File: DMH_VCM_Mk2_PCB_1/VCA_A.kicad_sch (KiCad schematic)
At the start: 19 parts, among them Q1 BC548, Q2 BC548, U1 TL074

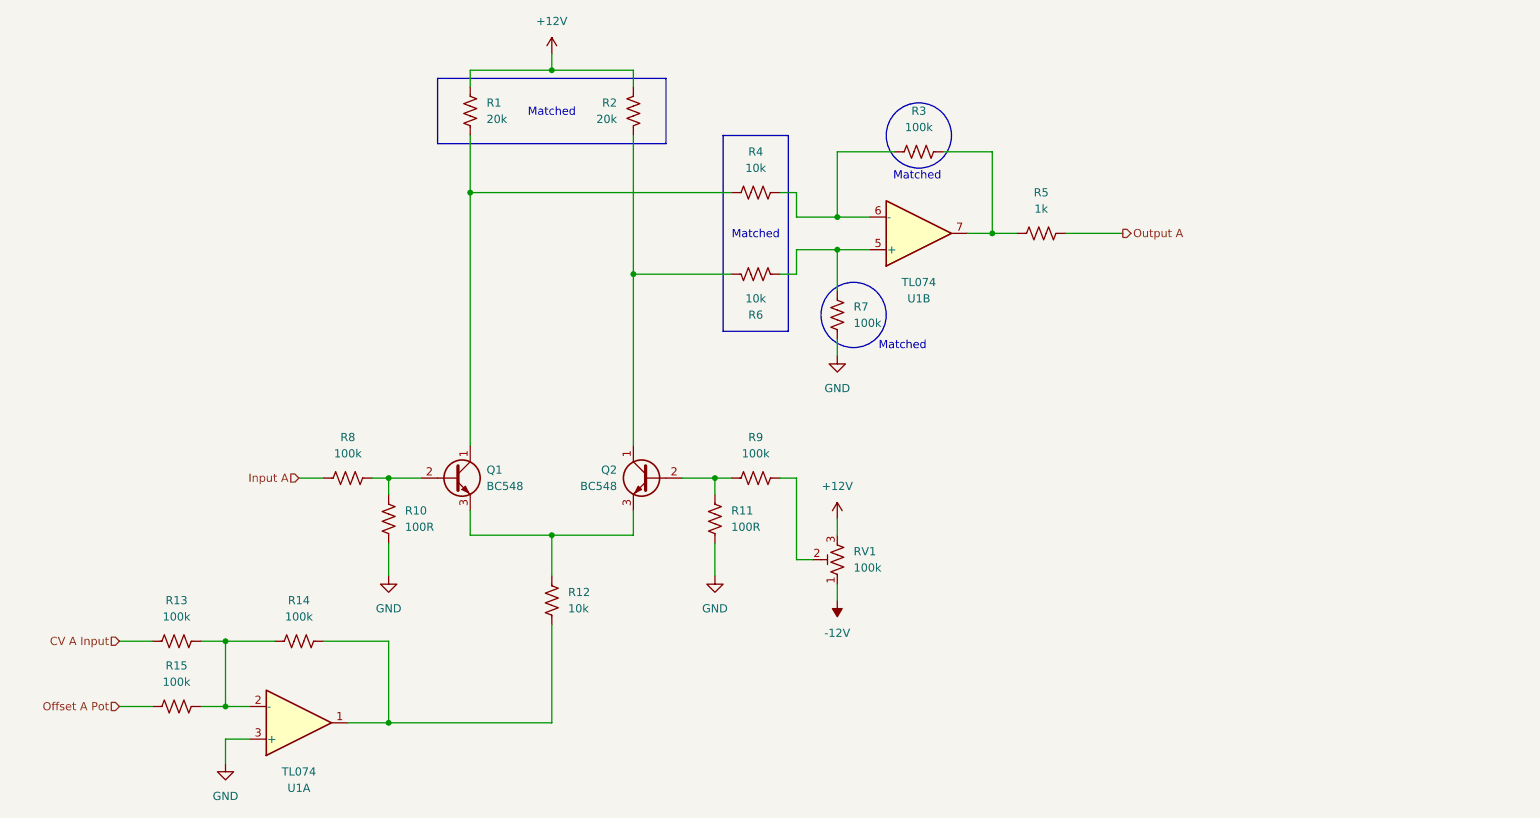
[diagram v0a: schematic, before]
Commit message: Almost finished PCB 1 schematic
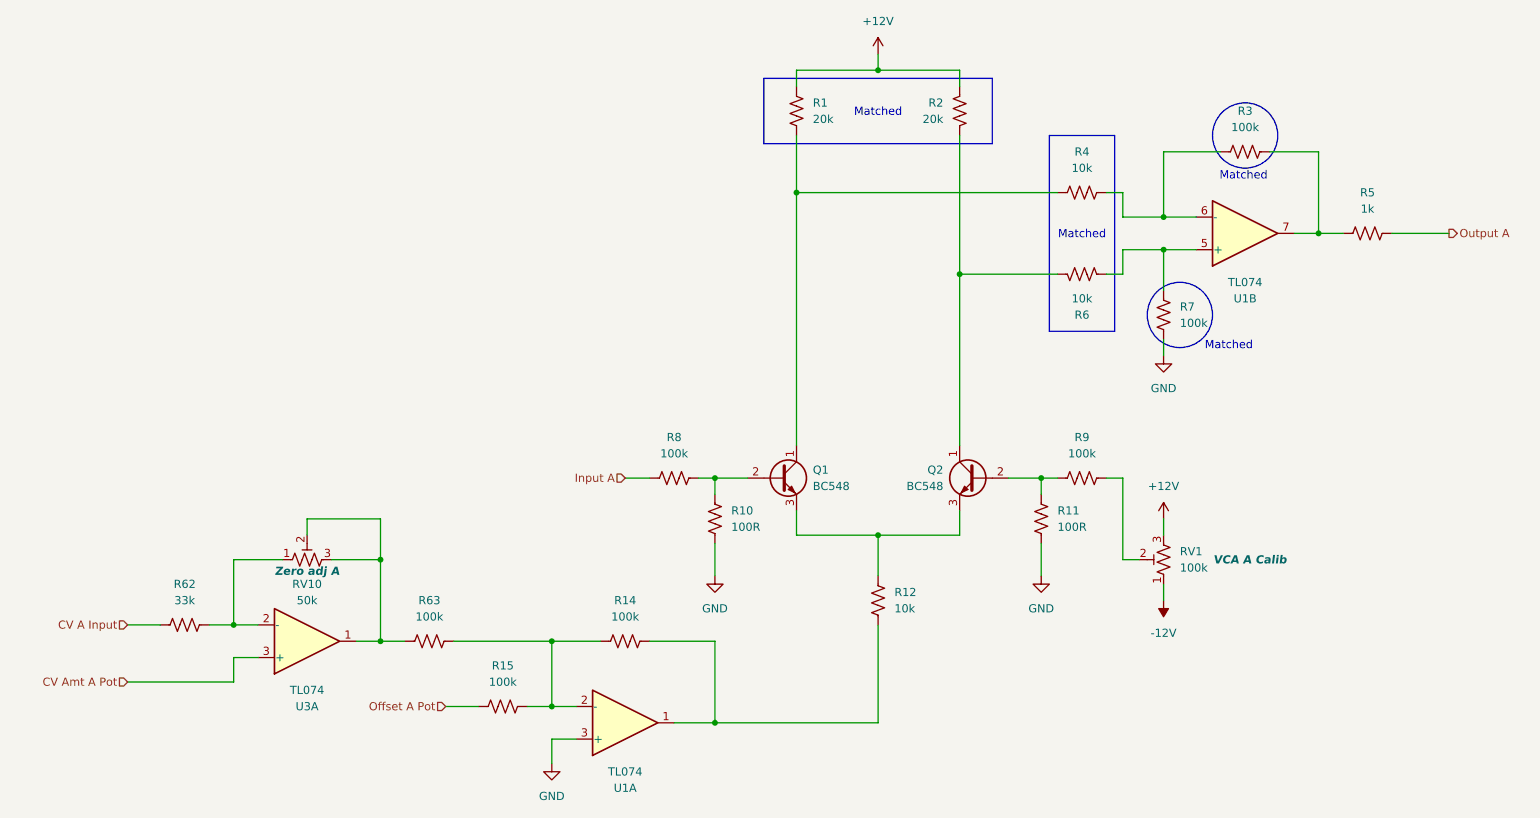
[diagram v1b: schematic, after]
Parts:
- removed R13: 100k, Resistor_THT:R_Axial_DIN0207_L6.3mm_D2.5mm_P2.54mm_Vertical, symbol Device:R_US
- added R62: 33k, Resistor_THT:R_Axial_DIN0207_L6.3mm_D2.5mm_P7.62mm_Horizontal, symbol Device:R_US
- added R63: 100k, Resistor_THT:R_Axial_DIN0207_L6.3mm_D2.5mm_P7.62mm_Horizontal, symbol Device:R_US
- added RV10: 50k, Potentiometer_THT:Potentiometer_Bourns_3296W_Vertical, symbol Device:R_Potentiometer_Trim_US
- added U3: TL074, Package_DIP:DIP-14_W7.62mm_Socket, symbol Amplifier_Operational:TL074
- RV1: Function (none) -> VCA A Calib
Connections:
- net CV A Input: now also R62.1
- net at R14.1, R15.2, U1.2 (-): now also R63.2
- new net: R63.1, RV10.2, RV10.3, U3.1
- new net: R62.2, RV10.1, U3.2 (-)
- new net CV Amt A Pot: U3.3 (+)
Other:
- moved on the sheet: Q1, Q2, R1, R10, R11, R12, R14, R15, R2, R3, R4, R5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

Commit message: PCB 1 placement in progress
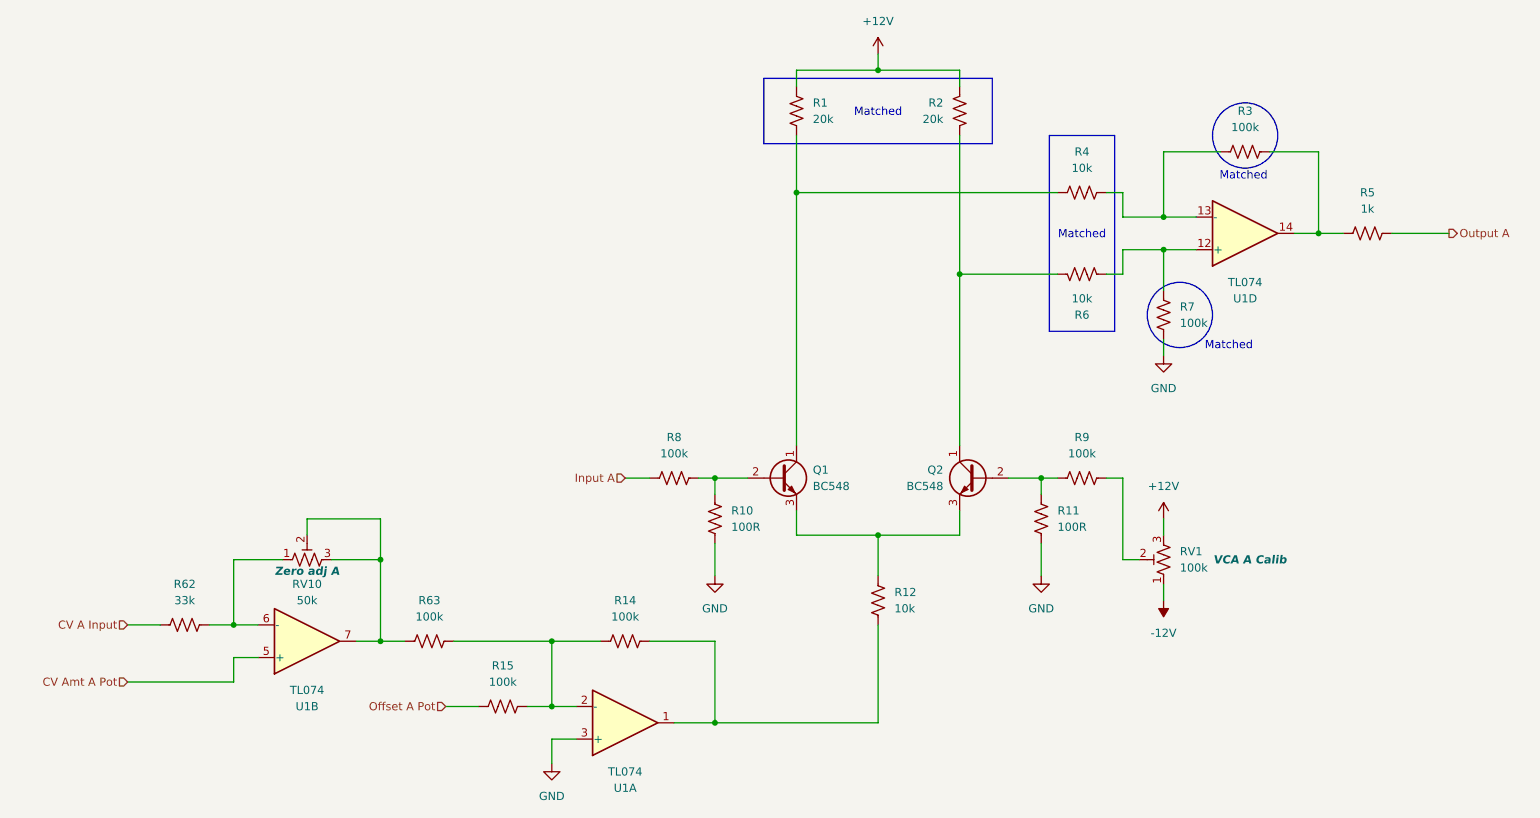
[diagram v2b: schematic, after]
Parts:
- R62, R63: footprint Resistor_THT:R_Axial_DIN0207_L6.3mm_D2.5mm_P7.62mm_Horizontal -> Resistor_THT:R_Axial_DIN0207_L6.3mm_D2.5mm_P2.54mm_Vertical
- renumbered U3 to U1
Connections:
- net CV Amt A Pot: now also U1.5 (+); no longer U1.3 (+)
- net at R3.1, R5.2: now also U1.14; no longer U1.7
- net at R3.2, R4.1: now also U1.13 (-); no longer U1.6 (-)
- net at R63.1, RV10.2, RV10.3: now also U1.7; no longer U1.1
- net at R62.2, RV10.1: now also U1.6 (-); no longer U1.2 (-)
- net at R6.1, R7.1: now also U1.12 (+); no longer U1.5 (+)
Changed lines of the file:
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@@
 		(at 88.9 139.7 0)
 		(mirror x)
-		(unit 1)
-		(exclude_from_sim no)
-		(in_bom yes)
-		(on_board yes)
-		(dnp no)
-		(property "Reference" "U3"
+		(unit 2)
+		(exclude_from_sim no)
+		(in_bom yes)
+		(on_board yes)
+		(dnp no)
+		(property "Reference" "U1"
 			(at 88.9 149.86 0)
 			(effects
@@
 			(project "DMH_VCM_Mk2_PCB_1"
 				(path "/58f4306d-5387-4983-bb08-41a2313fd315/7ad2d702-dfb7-4d49-a82d-34430dd5948f"
-					(reference "U3")
-					(unit 1)
+					(reference "U1")
+					(unit 2)
 				)
 			)
@@
 		(at 234.95 76.2 0)
 		(mirror x)
-		(unit 2)
+		(unit 4)
 		(exclude_from_sim no)
 		(in_bom yes)
@@
 				(path "/58f4306d-5387-4983-bb08-41a2313fd315/7ad2d702-dfb7-4d49-a82d-34430dd5948f"
 					(reference "U1")
-					(unit 2)
+					(unit 4)
 				)
 			)
@@
 			)
 		)
-		(property "Footprint" "Resistor_THT:R_Axial_DIN0207_L6.3mm_D2.5mm_P7.62mm_Horizontal"
+		(property "Footprint" "Resistor_THT:R_Axial_DIN0207_L6.3mm_D2.5mm_P2.54mm_Vertical"
 			(at 108.204 138.684 90)
 			(effects
@@
 			)
 		)
-		(property "Footprint" "Resistor_THT:R_Axial_DIN0207_L6.3mm_D2.5mm_P7.62mm_Horizontal"
+		(property "Footprint" "Resistor_THT:R_Axial_DIN0207_L6.3mm_D2.5mm_P2.54mm_Vertical"
 			(at 70.104 136.144 90)
 			(effects

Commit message: PCB 1 placement done
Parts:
- RV1: Function VCA A Calib -> Calib A
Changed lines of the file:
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@@
 			)
 		)
-		(property "Function" "VCA A Calib"
-			(at 235.712 127 0)
+		(property "Function" "Calib A"
+			(at 233.172 127 0)
 			(effects
 				(font
